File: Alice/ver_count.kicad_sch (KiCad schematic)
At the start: 315 parts, among them Q10 NOT_OC, Q100 NOT_OC, Q101 NOT_OC, Q102 NOT_OC, Q103 NOT_OC, Q104 NOT_OC, Q105 NOT_OC, Q106 NOT_OC, Q107 NOT_OC, Q108 NOT_OC, Q109 NOT_OC, Q11 NOT_OC, Q110 NOT_OC, Q111 NOT_OC, Q112 NOT_OC, Q113 NOT_OC, Q114 NOT_OC, Q115 NOT_OC, Q116 NOT_OC, Q117 NOT_OC, Q118 NOT_OC, Q119 NOT_OC, Q12 NOT_OC, Q120 NOT_OC, Q121 NOT_OC, Q122 NOT_OC, Q123 NOT_OC, Q124 NOT_OC, Q125 NOT_OC, Q126 NOT_OC, Q127 NOT_OC, Q128 NOT_OC, Q129 NOT_OC, Q13 NOT_OC, Q130 NOT_OC, Q131 NOT_OC, Q132 NOT_OC, Q133 NOT_OC, Q134 NOT_OC, Q135 NOT_OC, Q136 NOT_OC, Q137 NOT_OC, Q138 NOT_OC, Q139 NOT_OC, Q14 NOT_OC, Q140 NOT_OC, Q141 NOT_OC, Q142 NOT_OC, Q143 NOT_OC, Q144 NOT_OC, Q145 NOT_OC, Q146 NOT_OC, Q147 NOT_OC, Q148 NOT_OC, Q149 NOT_OC, Q15 NOT_OC, Q150 NOT_OC, Q151 NOT_OC, Q152 NOT_OC, Q153 NOT_OC, Q154 NOT_OC, Q155 NOT_OC, Q156 NOT_OC, Q157 NOT_OC, Q158 NOT_OC, Q16 NOT_OC, Q17 NOT_OC, Q18 NOT_OC, Q19 NOT_OC, Q20 NOT_OC, Q21 NOT_OC, Q22 NOT_OC, Q23 NOT_OC, Q24 NOT_OC, Q25 NOT_OC, Q26 NOT_OC, Q27 NOT_OC, Q270 NOT_OC, Q271 NOT_OC, Q272 NOT_OC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

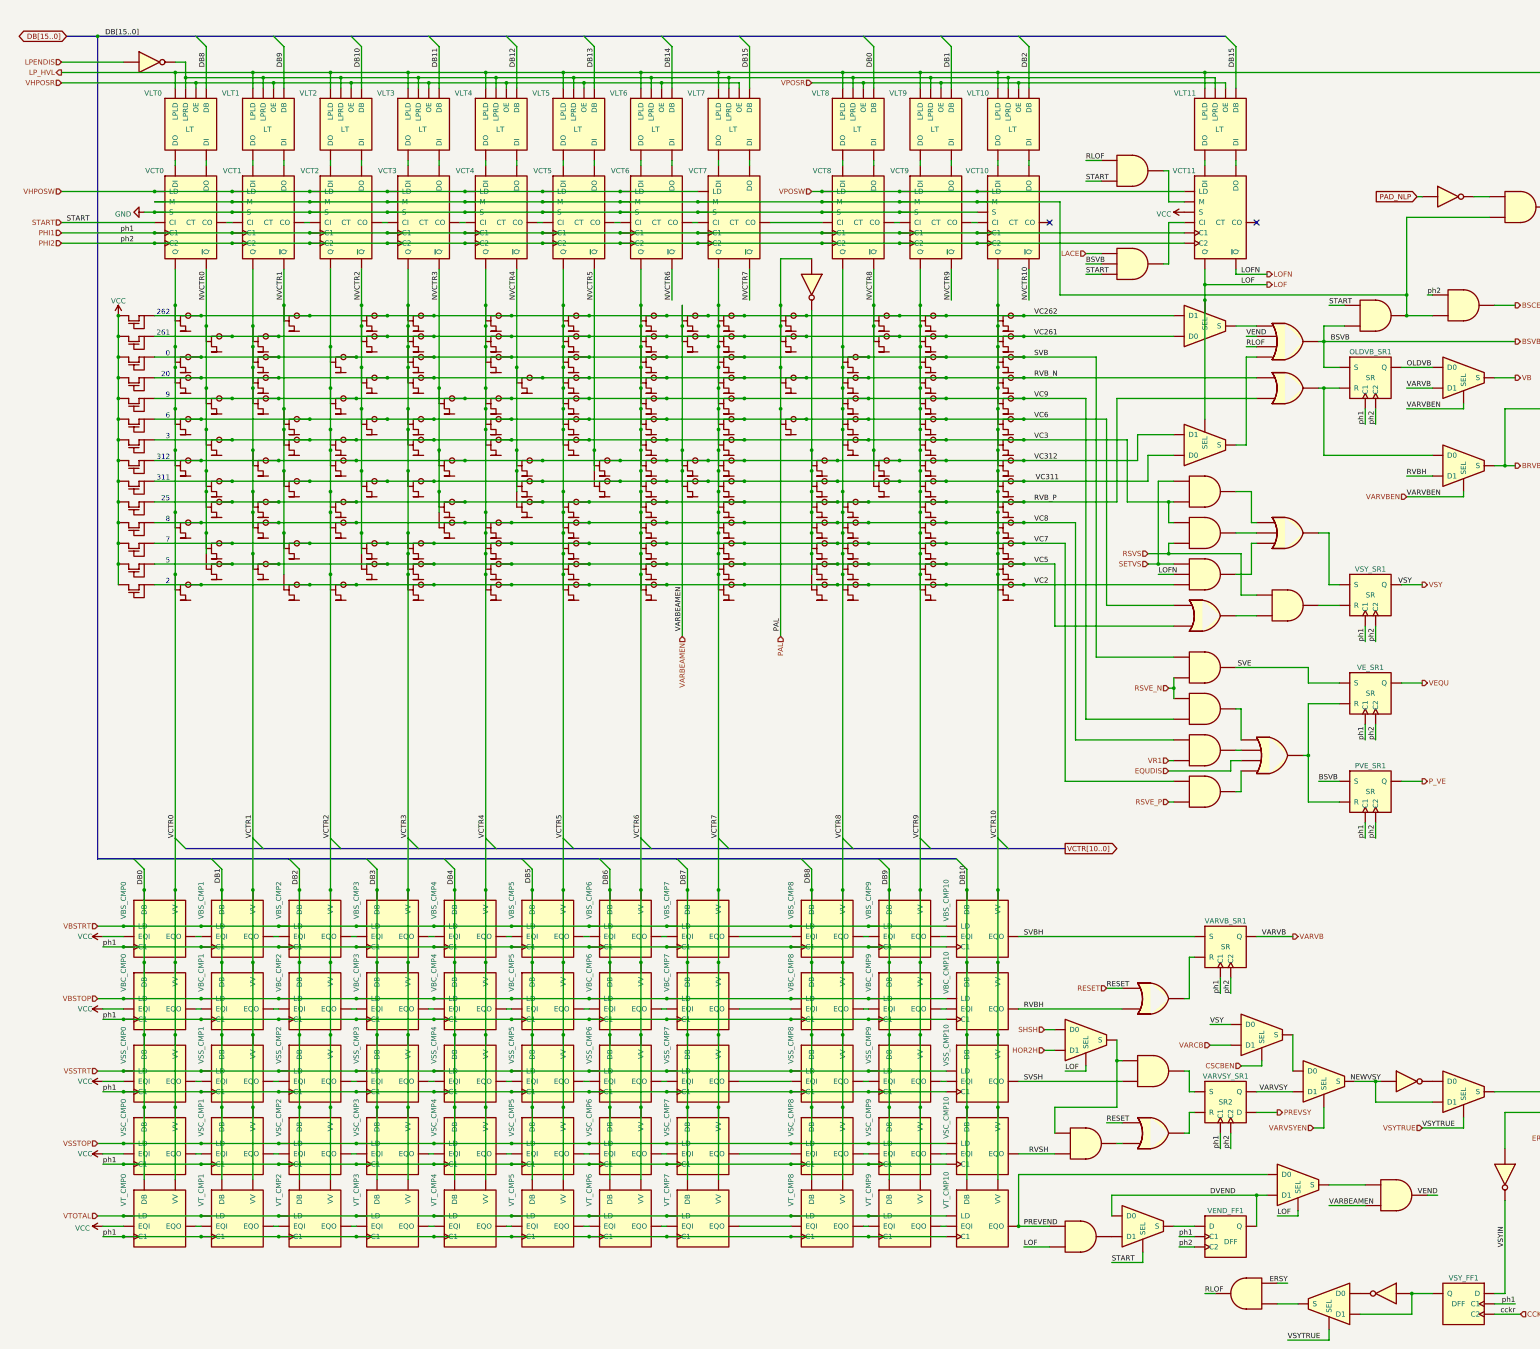
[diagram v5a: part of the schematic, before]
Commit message: Schematics have been annotated
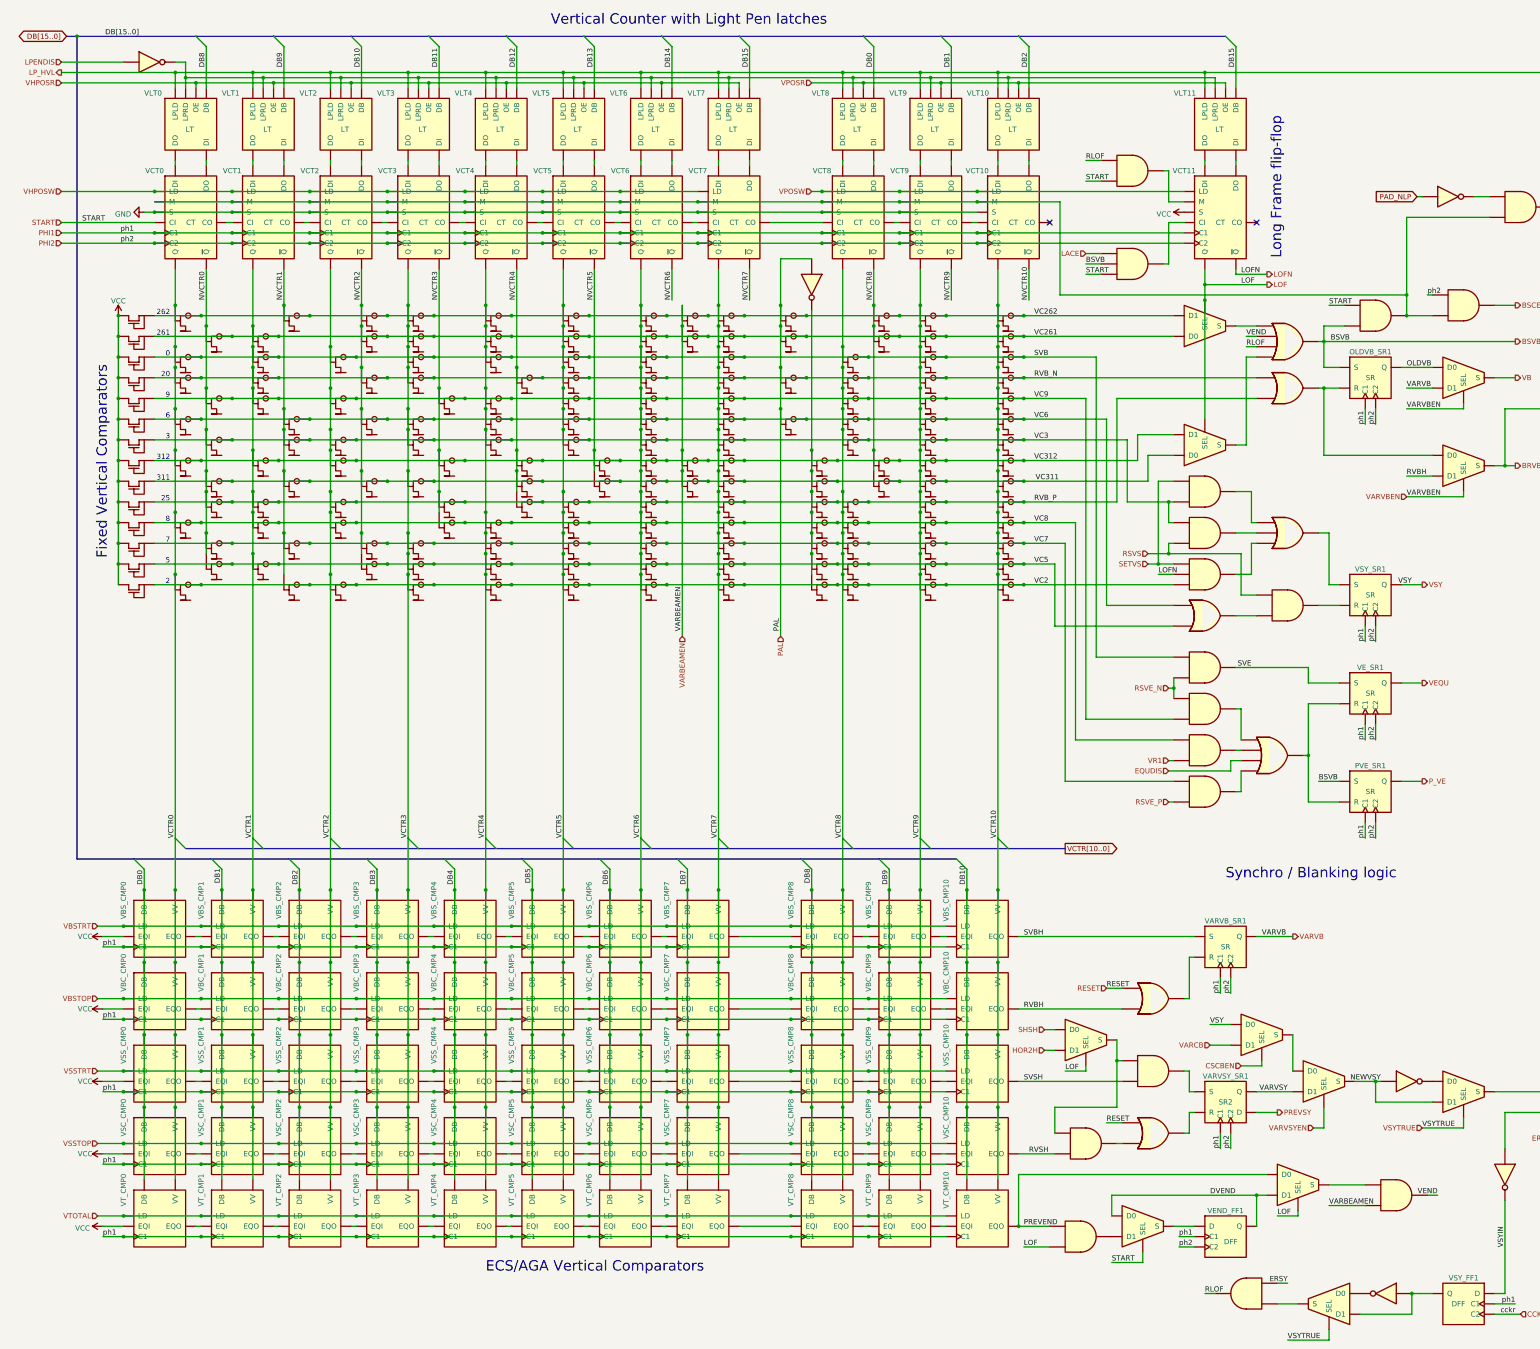
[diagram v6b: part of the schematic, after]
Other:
- note added: "ECS/AGA Vertical Comparators"
- note added: "Fixed Vertical Comparators"
- note added: "Long Frame flip-flop"
- note added: "Synchro / Blanking logic"
- note added: "Vertical Counter with Light Pen latches"
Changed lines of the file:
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@@
   (junction (at 172.72 247.65) (diameter 0) (color 0 0 0 0)
   )
-  (junction (at 33.02 24.13) (diameter 0) (color 0 0 0 0)
-  )
   (junction (at 254 140.97) (diameter 0) (color 0 0 0 0)
   )
@@
   (junction (at 142.24 128.27) (diameter 0) (color 0 0 0 0)
   )
+  (junction (at 27.94 24.13) (diameter 0) (color 0 0 0 0)
+  )
   (junction (at 207.01 118.11) (diameter 0) (color 0 0 0 0)
   )
@@
     (stroke (width 0) (type default) (color 0 0 0 0))
   )
-  (bus (pts (xy 33.02 226.06) (xy 41.91 226.06))
+  (bus (pts (xy 27.94 226.06) (xy 41.91 226.06))
     (stroke (width 0) (type default) (color 0 0 0 0))
   )
@@
     (stroke (width 0) (type default) (color 0 0 0 0))
   )
-  (bus (pts (xy 33.02 24.13) (xy 57.15 24.13))
+  (bus (pts (xy 27.94 24.13) (xy 57.15 24.13))
     (stroke (width 0) (type default) (color 0 0 0 0))
   )
@@
     (stroke (width 0) (type default) (color 0 0 0 0))
   )
-  (bus (pts (xy 33.02 24.13) (xy 33.02 226.06))
+  (bus (pts (xy 27.94 24.13) (xy 27.94 226.06))
     (stroke (width 0) (type default) (color 0 0 0 0))
   )
@@
     (stroke (width 0) (type default) (color 0 0 0 0))
   )
-  (bus (pts (xy 25.4 24.13) (xy 33.02 24.13))
+  (bus (pts (xy 25.4 24.13) (xy 27.94 24.13))
     (stroke (width 0) (type default) (color 0 0 0 0))
   )
@@
     (effects (font (size 1.27 1.27)) (justify right bottom))
   )
+  (text "ECS/AGA Vertical Comparators" (at 128.27 327.66 0)
+    (effects (font (size 2.54 2.54)) (justify left bottom))
+  )
   (text "CAS" (at 389.89 339.09 0)
     (effects (font (size 1.27 1.27)) (justify left bottom))
@@
     (effects (font (size 1.27 1.27)) (justify right bottom))
   )
+  (text "Vertical Counter with Light Pen latches" (at 212.09 21.59 180)
+    (effects (font (size 2.54 2.54)) (justify right bottom))
+  )
   (text "2" (at 50.8 158.75 180)
     (effects (font (size 1.27 1.27)) (justify right bottom))
   )
+  (text "Fixed Vertical Comparators" (at 35.56 152.4 90)
+    (effects (font (size 2.54 2.54)) (justify left bottom))
+  )
   (text "261\n" (at 50.8 97.79 180)
     (effects (font (size 1.27 1.27)) (justify right bottom))
   )
+  (text "Long Frame flip-flop" (at 323.85 78.74 90)
+    (effects (font (size 2.54 2.54)) (justify left bottom))
+  )
+  (text "Synchro / Blanking logic" (at 309.88 231.14 0)
+    (effects (font (size 2.54 2.54)) (justify left bottom))
+  )
   (text "9" (at 50.8 113.03 180)
     (effects (font (size 1.27 1.27)) (justify right bottom))
@@
     (effects (font (size 1.27 1.27)) (justify left bottom))
   )
-  (label "START" (at 25.4 69.85 0)
+  (label "START" (at 29.21 69.85 0)
     (effects (font (size 1.27 1.27)) (justify left bottom))
   )

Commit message: Copper DMA done
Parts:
- removed AND_39: AND2, symbol NMOS:AND2
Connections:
- net BSCE: now also AND_37.1, AND_40.3, VCT0.4 (M), VCT1.4 (M), VCT10.4 (M), VCT2.4 (M), VCT3.4 (M), VCT4.4 (M), VCT5.4 (M), VCT6.4 (M), VCT7.4 (M), VCT8.4 (M), VCT9.4 (M)
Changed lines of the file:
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@@
     (stroke (width 0) (type default) (color 0 0 0 0))
   )
-  (wire (pts (xy 359.41 87.63) (xy 360.68 87.63))
-    (stroke (width 0) (type default) (color 0 0 0 0))
-  )
   (wire (pts (xy 346.71 220.98) (xy 346.71 217.17))
     (stroke (width 0) (type default) (color 0 0 0 0))
@@
     (stroke (width 0) (type default) (color 0 0 0 0))
   )
-  (wire (pts (xy 375.92 90.17) (xy 381 90.17))
-    (stroke (width 0) (type default) (color 0 0 0 0))
-  )
   (wire (pts (xy 222.25 118.11) (xy 241.3 118.11))
     (stroke (width 0) (type default) (color 0 0 0 0))
@@
     (stroke (width 0) (type default) (color 0 0 0 0))
   )
-  (wire (pts (xy 360.68 92.71) (xy 354.33 92.71))
+  (wire (pts (xy 354.33 92.71) (xy 381 92.71))
     (stroke (width 0) (type default) (color 0 0 0 0))
   )
@@
     (effects (font (size 1.27 1.27)) (justify left bottom))
   )
-  (label "ph2" (at 359.41 87.63 0)
-    (effects (font (size 1.27 1.27)) (justify left bottom))
-  )
   (label "VSYTRUE" (at 358.14 292.1 0)
     (effects (font (size 1.27 1.27)) (justify left bottom))
@@
     (effects (font (size 1.27 1.27)) (justify right))
   )
-  (hierarchical_label "BSCE" (shape output) (at 381 90.17 0)
+  (hierarchical_label "BSCE" (shape output) (at 381 92.71 0)
     (effects (font (size 1.27 1.27)) (justify left))
   )
@@
     (pin "9")
   )
-  (symbol (lib_id "NMOS:AND2") (at 368.3 90.17 0) (unit 1)
-    (in_bom yes) (on_board yes) (fields_autoplaced)
-    (property "Reference" "AND_39" (id 0) (at 368.3 90.17 0)
-      (effects (font (size 1.27 1.27)) hide)
-    )
-    (property "Value" "AND2" (id 1) (at 368.3 95.25 0)
-      (effects (font (size 1.27 1.27)) hide)
-    )
-    (property "Footprint" "" (id 2) (at 368.3 90.17 0)
-      (effects (font (size 1.27 1.27)) hide)
-    )
-    (property "Datasheet" "" (id 3) (at 368.3 90.17 0)
-      (effects (font (size 1.27 1.27)) hide)
-    )
-    (pin "1")
-    (pin "2")
-    (pin "3")
-  )
   (symbol (lib_id "NMOS:NOT_OC") (at 116.84 114.3 0) (unit 1)
